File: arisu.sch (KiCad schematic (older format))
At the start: 26 parts, among them J1 USB_B_Micro, U1 USBLC6-2SC6, U2 ATmega32U4-AU, Y1 Crystal_GND24

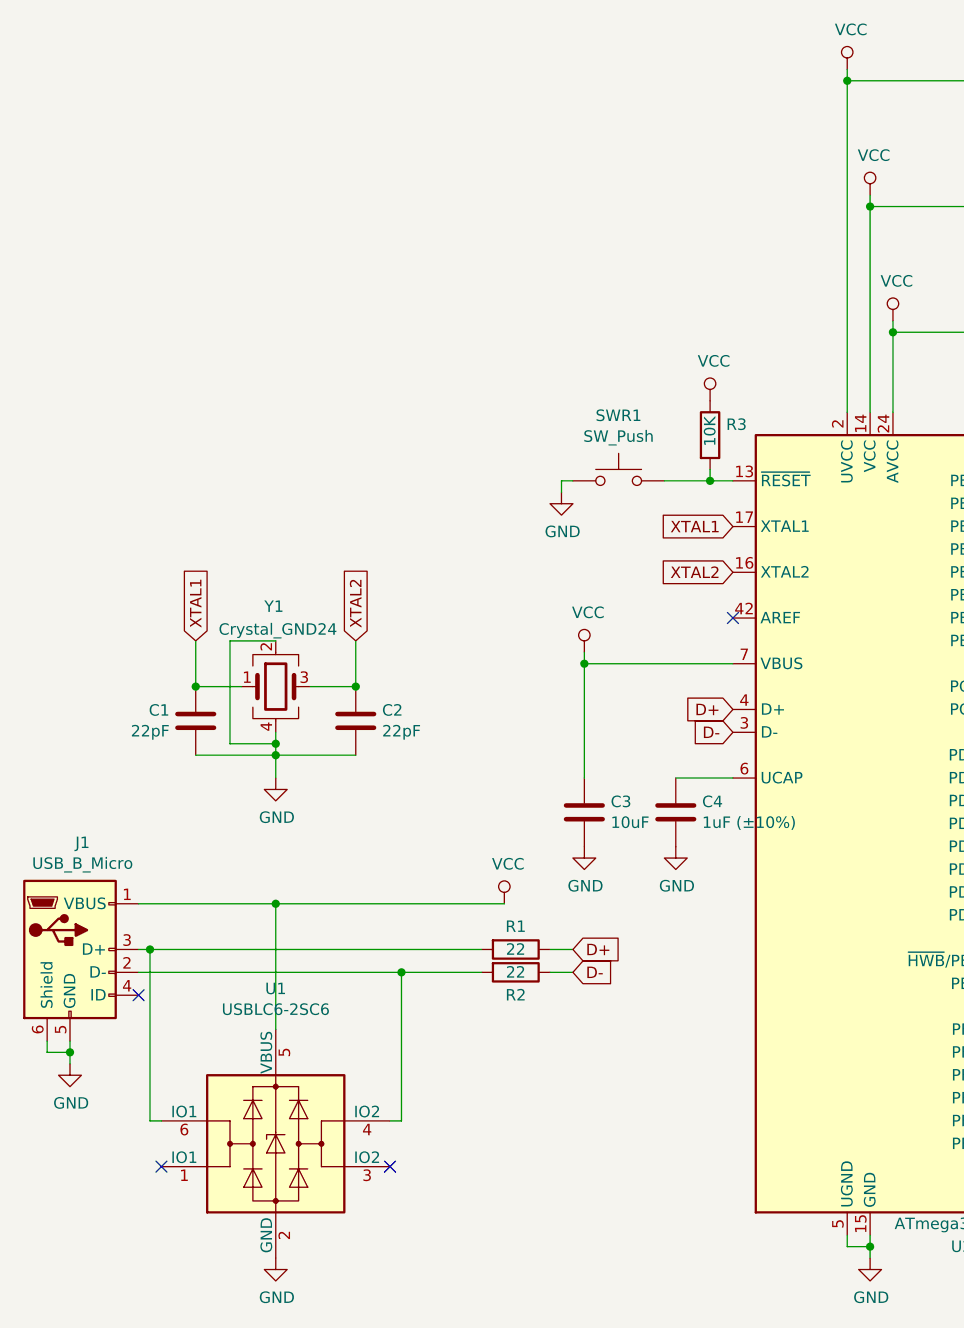
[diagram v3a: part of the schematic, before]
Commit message: Swap out micro-USB for USB-C 2.0
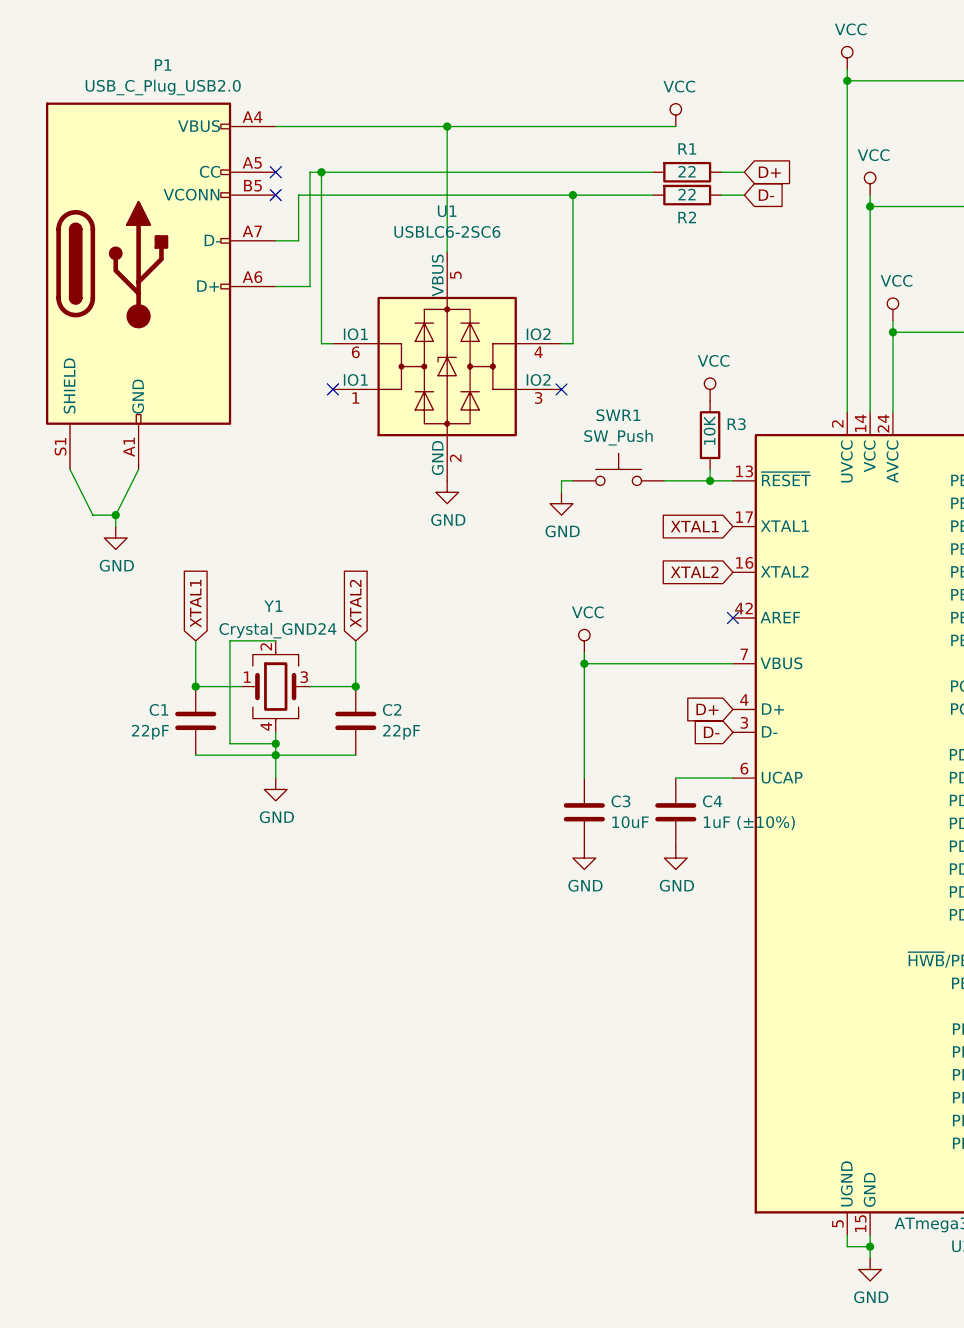
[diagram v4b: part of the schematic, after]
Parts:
- removed J1: USB_B_Micro, Connectors_USB:USB_Micro-B_Molex-105017-0001, symbol Connector:USB_B_Micro
- added P1: USB_C_Plug_USB2.0, Connector_USB:USB_C_Receptacle_GCT_USB4085, symbol Connector:USB_C_Plug_USB2.0
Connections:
- net GND: now also P1.A1 (GND), P1.A12 (GND), P1.B1 (GND), P1.B12 (GND), P1.S1 (SHIELD)
- net VCC: now also P1.A4 (VBUS), P1.A9 (VBUS), P1.B4 (VBUS), P1.B9 (VBUS)
- net at R2.2, U1.4 (IO2): now also P1.A7 (D-)
- net at R1.2, U1.6 (IO1): now also P1.A6 (D+)
- no-connect marks 12 -> 13
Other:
- moved on the sheet: R1, R2, U1
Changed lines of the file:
@@
-$EndComp
-$Comp
-L Connector:USB_B_Micro J1
-U 1 1 5C4B21E5
-P 1000 4800
-F 0 "J1" H 1055 5267 50  0000 C CNN
-F 1 "USB_B_Micro" H 1055 5176 50  0000 C CNN
-F 2 "Connectors_USB:USB_Micro-B_Molex-105017-0001" H 1150 4750 50  0001 C CNN
-F 3 "~" H 1150 4750 50  0001 C CNN
-	1    1000 4800
-	1    0    0    -1
-$EndComp
-$Comp
-L Power_Protection:USBLC6-2SC6 U1
-U 1 1 5C4B2347
-P 1900 5650
-F 0 "U1" H 1900 6328 50  0000 C CNN
-F 1 "USBLC6-2SC6" H 1900 6237 50  0000 C CNN
-F 2 "TO_SOT_Packages_SMD:SOT-23-6_Handsoldering" H 1150 6050 50  0001 C CNN
-F 3 "http://www2.st.com/resource/en/datasheet/CD00050750.pdf" H 2100 6000 50  0001 C CNN
-	1    1900 5650
-	1    0    0    -1
 $EndComp
 $Comp
 L Device:R R1
 U 1 1 5C4B245D
-P 2950 4800
-F 0 "R1" V 2850 4800 50  0000 C CNN
-F 1 "22" V 2950 4800 50  0000 C CNN
-F 2 "Resistors_SMD:R_0805_HandSoldering" V 2880 4800 50  0001 C CNN
-F 3 "~" H 2950 4800 50  0001 C CNN
-	1    2950 4800
+P 3700 1400
+F 0 "R1" V 3600 1400 50  0000 C CNN
+F 1 "22" V 3700 1400 50  0000 C CNN
+F 2 "Resistors_SMD:R_0805_HandSoldering" V 3630 1400 50  0001 C CNN
+F 3 "~" H 3700 1400 50  0001 C CNN
+	1    3700 1400
 	0    1    1    0
 $EndComp
@@
 L Device:R R2
 U 1 1 5C4B25B0
-P 2950 4900
-F 0 "R2" V 3050 4900 50  0000 C CNN
-F 1 "22" V 2950 4900 50  0000 C CNN
-F 2 "Resistors_SMD:R_0805_HandSoldering" V 2880 4900 50  0001 C CNN
-F 3 "~" H 2950 4900 50  0001 C CNN
-	1    2950 4900
+P 3700 1500
+F 0 "R2" V 3800 1500 50  0000 C CNN
+F 1 "22" V 3700 1500 50  0000 C CNN
+F 2 "Resistors_SMD:R_0805_HandSoldering" V 3630 1500 50  0001 C CNN
+F 3 "~" H 3700 1500 50  0001 C CNN
+	1    3700 1500
 	0    1    1    0
 $EndComp
 Wire Wire Line
-	1300 4600 1900 4600
+	1900 1200 2650 1200
 $Comp
 L power:VCC #PWR0101
 U 1 1 5C4B2712
-P 2900 4600
-F 0 "#PWR0101" H 2900 4450 50  0001 C CNN
-F 1 "VCC" H 2917 4773 50  0000 C CNN
-F 2 "" H 2900 4600 50  0001 C CNN
-F 3 "" H 2900 4600 50  0001 C CNN
-	1    2900 4600
-	1    0    0    -1
-$EndComp
-Wire Wire Line
-	1900 4600 1900 5150
-Connection ~ 1900 4600
-Text GLabel 3200 4800 2    50   Input ~ 0
+P 3650 1200
+F 0 "#PWR0101" H 3650 1050 50  0001 C CNN
+F 1 "VCC" H 3667 1373 50  0000 C CNN
+F 2 "" H 3650 1200 50  0001 C CNN
+F 3 "" H 3650 1200 50  0001 C CNN
+	1    3650 1200
+	1    0    0    -1
+$EndComp
+Wire Wire Line
+	2650 1200 2650 1750
+Connection ~ 2650 1200
+Text GLabel 3950 1400 2    50   Input ~ 0
 D+
 Wire Wire Line
-	3100 4800 3200 4800
-Text GLabel 3200 4900 2    50   Input ~ 0
+	3850 1400 3950 1400
+Text GLabel 3950 1500 2    50   Input ~ 0
 D-
 Wire Wire Line
-	3100 4900 3200 4900
-Wire Wire Line
-	1300 4800 1350 4800
-Wire Wire Line
-	1400 5550 1350 5550
-Wire Wire Line
-	1350 5550 1350 4800
-Connection ~ 1350 4800
-Wire Wire Line
-	1300 4900 2450 4900
-Wire Wire Line
-	2400 5550 2450 5550
-Wire Wire Line
-	2450 5550 2450 4900
-Connection ~ 2450 4900
+	3850 1500 3950 1500
+Wire Wire Line
+	2150 2150 2100 2150
+Wire Wire Line
+	3150 2150 3200 2150
+Wire Wire Line
+	3200 2150 3200 1500
 $Comp
 L power:GND #PWR0102
 U 1 1 5C4B3104
-P 1000 5300
-F 0 "#PWR0102" H 1000 5050 50  0001 C CNN
-F 1 "GND" H 1005 5127 50  0000 C CNN
-F 2 "" H 1000 5300 50  0001 C CNN
-F 3 "" H 1000 5300 50  0001 C CNN
-	1    1000 5300
-	1    0    0    -1
-$EndComp
-Wire Wire Line
-	900  5200 900  5250
-Wire Wire Line
-	900  5250 1000 5250
-Wire Wire Line
-	1000 5250 1000 5300
-Wire Wire Line
-	1000 5200 1000 5250
-Connection ~ 1000 5250
+P 1200 2950
+F 0 "#PWR0102" H 1200 2700 50  0001 C CNN
+F 1 "GND" H 1205 2777 50  0000 C CNN
+F 2 "" H 1200 2950 50  0001 C CNN
+F 3 "" H 1200 2950 50  0001 C CNN
+	1    1200 2950
+	1    0    0    -1
+$EndComp
+Wire Wire Line
+	1000 2700 1100 2900
+Wire Wire Line
+	1100 2900 1200 2900
+Wire Wire Line
+	1200 2900 1200 2950
+Wire Wire Line
+	1300 2700 1200 2900
+Connection ~ 1200 2900
 $Comp
 L power:GND #PWR0103
 U 1 1 5C4B33A3
-P 1900 6150
-F 0 "#PWR0103" H 1900 5900 50  0001 C CNN
-F 1 "GND" H 1905 5977 50  0000 C CNN
-F 2 "" H 1900 6150 50  0001 C CNN
-F 3 "" H 1900 6150 50  0001 C CNN
-	1    1900 6150
+P 2650 2750
+F 0 "#PWR0103" H 2650 2500 50  0001 C CNN
+F 1 "GND" H 2655 2577 50  0000 C CNN
+F 2 "" H 2650 2750 50  0001 C CNN
+F 3 "" H 2650 2750 50  0001 C CNN
+	1    2650 2750
 	1    0    0    -1
 $EndComp
@@
 Text Label 7200 3100 0    50   ~ 0
 row3
-NoConn ~ 1300 5000
-NoConn ~ 1400 5750
-NoConn ~ 2400 5750
+NoConn ~ 2150 2350
+NoConn ~ 3150 2350
 $Comp
 L Mechanical:MountingHole H1
@@
 NoConn ~ 5100 2950
 Wire Wire Line
-	1900 4600 2900 4600
-Wire Wire Line
-	1350 4800 2800 4800
-Wire Wire Line
-	2450 4900 2800 4900
+	2650 1200 3650 1200
 NoConn ~ 5100 3050
+$Comp
+L Connector:USB_C_Plug_USB2.0 P1
+U 1 1 5D65F9CC
+P 1300 1800
+F 0 "P1" H 1407 2667 50  0000 C CNN
+F 1 "USB_C_Plug_USB2.0" H 1407 2576 50  0000 C CNN
+F 2 "Connector_USB:USB_C_Receptacle_GCT_USB4085" H 1450 1800 50  0001 C CNN
+F 3 "https://www.usb.org/sites/default/files/documents/usb_type-c.zip" H 1450 1800 50  0001 C CNN
+	1    1300 1800
+	1    0    0    -1
+$EndComp
+Wire Wire Line
+	2000 1500 2000 1700
+Wire Wire Line
+	2000 1700 1900 1700
+Wire Wire Line
+	2000 1500 3200 1500
+Wire Wire Line
+	2050 1900 1900 1900
+$Comp
+L Power_Protection:USBLC6-2SC6 U1
+U 1 1 5C4B2347
+P 2650 2250
+F 0 "U1" H 2650 2928 50  0000 C CNN
+F 1 "USBLC6-2SC6" H 2650 2837 50  0000 C CNN
+F 2 "TO_SOT_Packages_SMD:SOT-23-6_Handsoldering" H 1900 2650 50  0001 C CNN
+F 3 "http://www2.st.com/resource/en/datasheet/CD00050750.pdf" H 2850 2600 50  0001 C CNN
+	1    2650 2250
+	1    0    0    -1
+$EndComp
+Connection ~ 3200 1500
+Wire Wire Line
+	3200 1500 3550 1500
+Wire Wire Line
+	2050 1400 2050 1900
+Wire Wire Line
+	2100 1400 3550 1400
+Connection ~ 2100 1400
+Wire Wire Line
+	2100 2150 2100 1400
+Wire Wire Line
+	2050 1400 2100 1400
+NoConn ~ 1900 1400
+NoConn ~ 1900 1500
+Wire Bus Line
+	7050 2650 7050 5800
 Wire Bus Line
 	6750 2750 6750 5800
-Wire Bus Line
-	7050 2650 7050 5800
 $EndSCHEMATC

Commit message: Route more traces.
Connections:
- net col7: now also U2.19 (PD1); no longer U2.9 (PB1)
- net col8: now also U2.18 (PD0); no longer U2.8 (PB0)
- net row0: now also U2.8 (PB0); no longer U2.18 (PD0)
- net row1: now also U2.9 (PB1); no longer U2.19 (PD1)
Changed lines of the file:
@@
 Entry Wire Line
 	6650 5250 6750 5350
-Text Label 6450 3950 0    50   ~ 0
+Text Label 6450 2750 0    50   ~ 0
 row0
-Text Label 6450 4050 0    50   ~ 0
+Text Label 6450 2850 0    50   ~ 0
 row1
 Text Label 6450 4150 0    50   ~ 0
@@
 Text Label 6450 4350 0    50   ~ 0
 col6
-Text Label 6450 2850 0    50   ~ 0
+Text Label 6450 4050 0    50   ~ 0
 col7
-Text Label 6450 2750 0    50   ~ 0
+Text Label 6450 3950 0    50   ~ 0
 col8
 Text Label 6450 3450 0    50   ~ 0

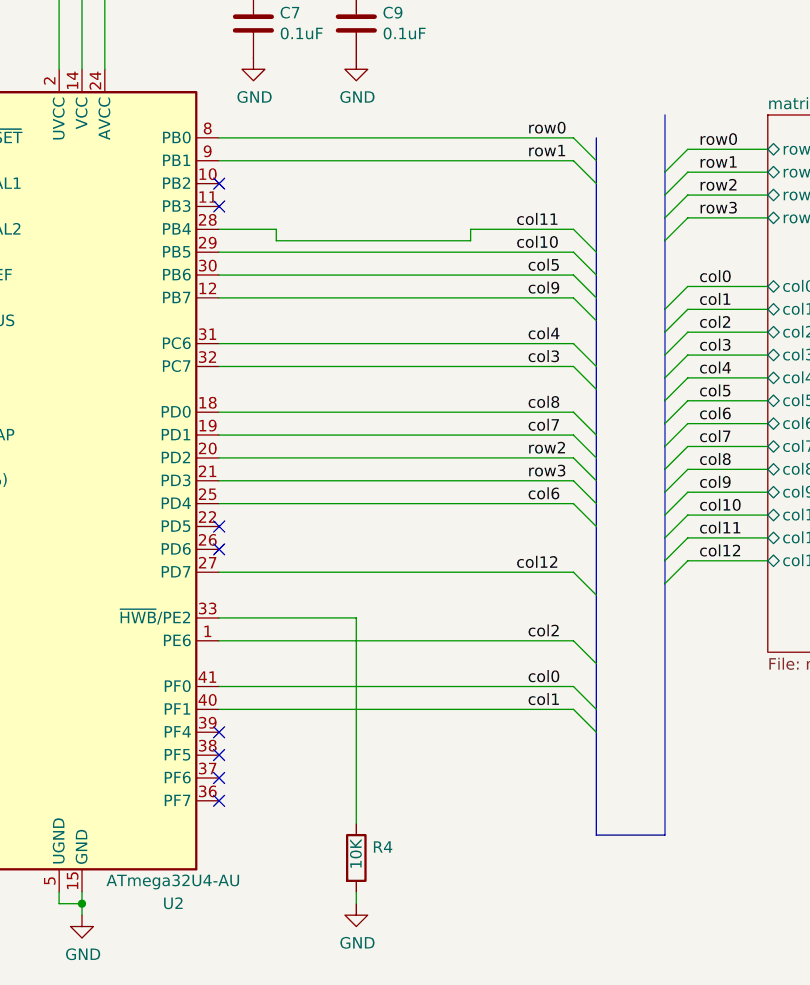
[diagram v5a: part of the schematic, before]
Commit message: Route a bunch of columns.
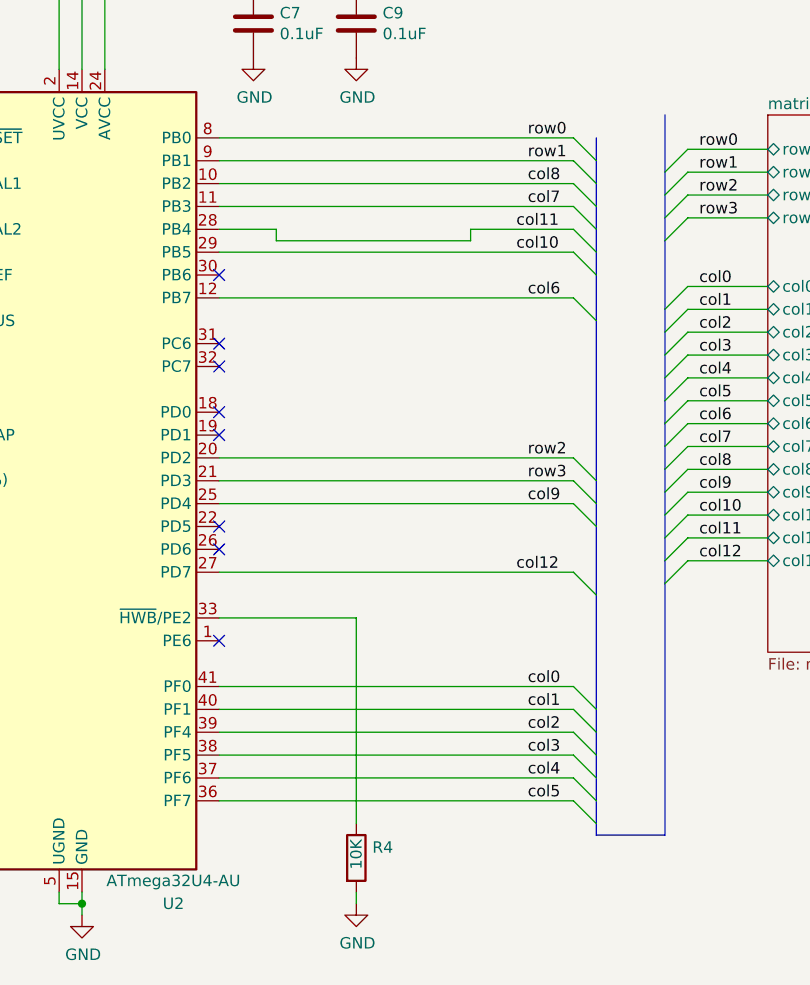
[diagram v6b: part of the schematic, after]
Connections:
- net col2: now also U2.39 (PF4); no longer U2.1 (PE6)
- net col3: now also U2.38 (PF5); no longer U2.32 (PC7)
- net col4: now also U2.37 (PF6); no longer U2.31 (PC6)
- net col5: now also U2.36 (PF7); no longer U2.30 (PB6)
- net col6: now also U2.12 (PB7); no longer U2.25 (PD4)
- net col7: now also U2.11 (PB3); no longer U2.19 (PD1)
- net col8: now also U2.10 (PB2); no longer U2.18 (PD0)
- net col9: now also U2.25 (PD4); no longer U2.12 (PB7)
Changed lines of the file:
@@
 	6650 3250 6750 3350
 Entry Wire Line
-	6650 3350 6750 3450
+	6650 5650 6750 5750
 Entry Wire Line
 	6650 3450 6750 3550
@@
 	5100 4650 6650 4650
 Entry Wire Line
-	6650 3650 6750 3750
-Entry Wire Line
-	6650 3750 6750 3850
-Entry Wire Line
-	6650 3950 6750 4050
-Entry Wire Line
-	6650 4050 6750 4150
+	6650 5350 6750 5450
+Entry Wire Line
+	6650 5450 6750 5550
+Entry Wire Line
+	6650 2950 6750 3050
+Entry Wire Line
+	6650 3050 6750 3150
 Entry Wire Line
 	6650 4150 6750 4250
@@
 	6650 2750 6750 2850
 Entry Wire Line
-	6650 4950 6750 5050
+	6650 5550 6750 5650
 Entry Wire Line
 	6650 5150 6750 5250
@@
 Text Label 6450 5250 0    50   ~ 0
 col1
-Text Label 6450 4950 0    50   ~ 0
+Text Label 6450 5350 0    50   ~ 0
 col2
-Text Label 6450 3750 0    50   ~ 0
+Text Label 6450 5450 0    50   ~ 0
 col3
-Text Label 6450 3650 0    50   ~ 0
+Text Label 6450 5550 0    50   ~ 0
 col4
-Text Label 6450 3350 0    50   ~ 0
+Text Label 6450 5650 0    50   ~ 0
 col5
+Text Label 6450 3450 0    50   ~ 0
+col6
+Text Label 6450 3050 0    50   ~ 0
+col7
+Text Label 6450 2950 0    50   ~ 0
+col8
 Text Label 6450 4350 0    50   ~ 0
-col6
-Text Label 6450 4050 0    50   ~ 0
-col7
-Text Label 6450 3950 0    50   ~ 0
-col8
-Text Label 6450 3450 0    50   ~ 0
 col9
 Text Label 6400 3250 0    50   ~ 0
@@
 	5100 3250 6650 3250
 Wire Wire Line
-	5100 3350 6650 3350
+	5100 5650 6650 5650
 Wire Wire Line
 	5100 3450 6650 3450
 Wire Wire Line
-	5100 3650 6650 3650
-Wire Wire Line
-	5100 3750 6650 3750
-Wire Wire Line
-	5100 3950 6650 3950
-Wire Wire Line
-	5100 4050 6650 4050
-Wire Wire Line
-	5100 4950 6650 4950
+	5100 5350 6650 5350
+Wire Wire Line
+	5100 5450 6650 5450
+Wire Wire Line
+	5100 2950 6650 2950
+Wire Wire Line
+	5100 3050 6650 3050
+Wire Wire Line
+	5100 5550 6650 5550
 Wire Wire Line
 	5100 5150 6650 5150
@@
 Wire Wire Line
 	5100 2850 6650 2850
-NoConn ~ 5100 5650
-NoConn ~ 5100 5550
-NoConn ~ 5100 5450
-NoConn ~ 5100 5350
-NoConn ~ 5100 2950
+NoConn ~ 5100 3350
+NoConn ~ 5100 4950
+NoConn ~ 5100 3750
+NoConn ~ 5100 3650
+NoConn ~ 5100 3950
 Wire Wire Line
 	2650 1200 3650 1200
-NoConn ~ 5100 3050
+NoConn ~ 5100 4050
 $Comp
 L Connector:USB_C_Plug_USB2.0 P1

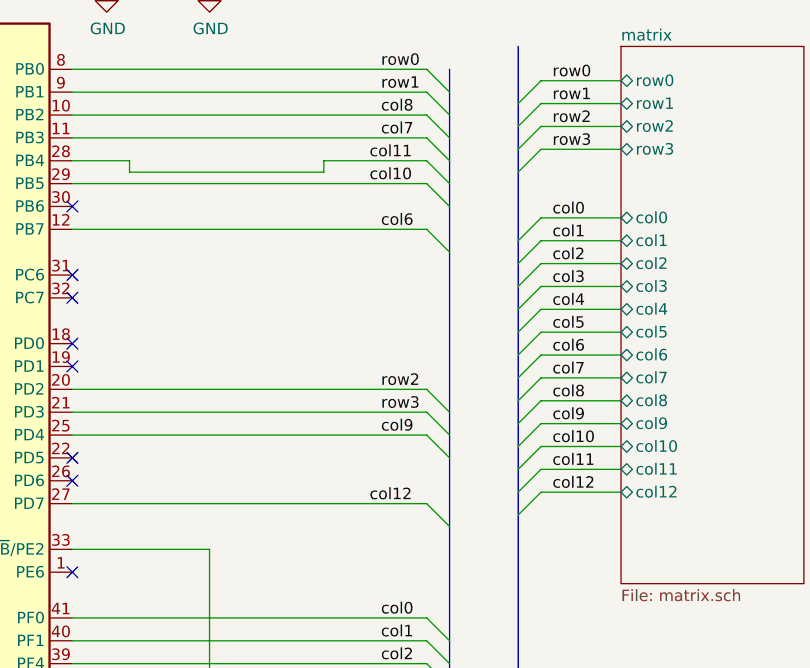
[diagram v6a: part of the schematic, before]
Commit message: Almost finish initial routing and board edge cuts.
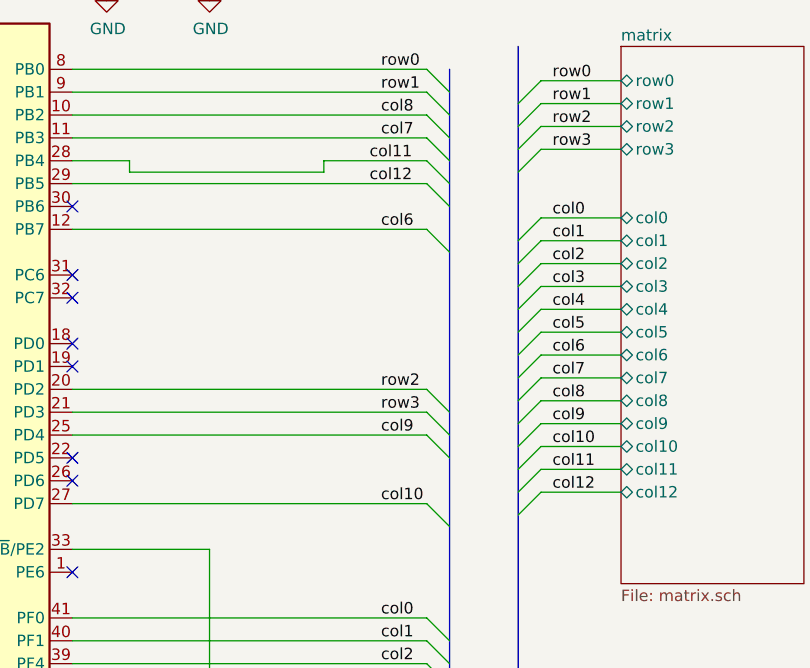
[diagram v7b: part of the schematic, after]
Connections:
- net col10: now also U2.27 (PD7); no longer U2.29 (PB5)
- net col12: now also U2.29 (PB5); no longer U2.27 (PD7)
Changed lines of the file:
@@
 	6650 5450 6750 5550
-Entry Wire Line
-	6650 2950 6750 3050
 Entry Wire Line
 	6650 3050 6750 3150
@@
 Text Label 6450 2850 0    50   ~ 0
 row1
-Text Label 6450 4150 0    50   ~ 0
-row2
-Text Label 6450 4250 0    50   ~ 0
-row3
 Text Label 6450 5150 0    50   ~ 0
 col0
@@
 Text Label 6450 5650 0    50   ~ 0
 col5
-Text Label 6450 3450 0    50   ~ 0
-col6
-Text Label 6450 3050 0    50   ~ 0
-col7
-Text Label 6450 2950 0    50   ~ 0
-col8
 Text Label 6450 4350 0    50   ~ 0
 col9
-Text Label 6400 3250 0    50   ~ 0
+Text Label 6450 4650 0    50   ~ 0
 col10
 Text Label 6400 3150 0    50   ~ 0
 col11
-Text Label 6400 4650 0    50   ~ 0
+Text Label 6400 3250 0    50   ~ 0
 col12
 $Comp
@@
 Wire Wire Line
 	5100 5450 6650 5450
-Wire Wire Line
-	5100 2950 6650 2950
 Wire Wire Line
 	5100 3050 6650 3050
@@
 	1    0    0    -1
 $EndComp
-NoConn ~ 5100 4450
 NoConn ~ 5100 4550
 Wire Wire Line
@@
 NoConn ~ 1900 1400
 NoConn ~ 1900 1500
+NoConn ~ 5100 4450
+Entry Wire Line
+	6650 2950 6750 3050
 Wire Bus Line
 	7050 2650 7050 5800
 Wire Bus Line
 	6750 2750 6750 5800
+Wire Wire Line
+	5100 2950 6650 2950
+Text Label 6450 2950 0    50   ~ 0
+col8
+Text Label 6450 4250 0    50   ~ 0
+row3
+Text Label 6450 3050 0    50   ~ 0
+col7
+Text Label 6450 3450 0    50   ~ 0
+col6
+Text Label 6450 4150 0    50   ~ 0
+row2
 $EndSCHEMATC
